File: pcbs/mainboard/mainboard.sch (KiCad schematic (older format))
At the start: 32 parts, among them J1 USB_B_Micro, SW1 SW_Push, SW2 SW_Push, U1 ATmega32U4-AU, U2 USBLC6-2SC6, U3 XC6206P332MR, U4 XC9572XL-10VQG44C, Y1 16MHz

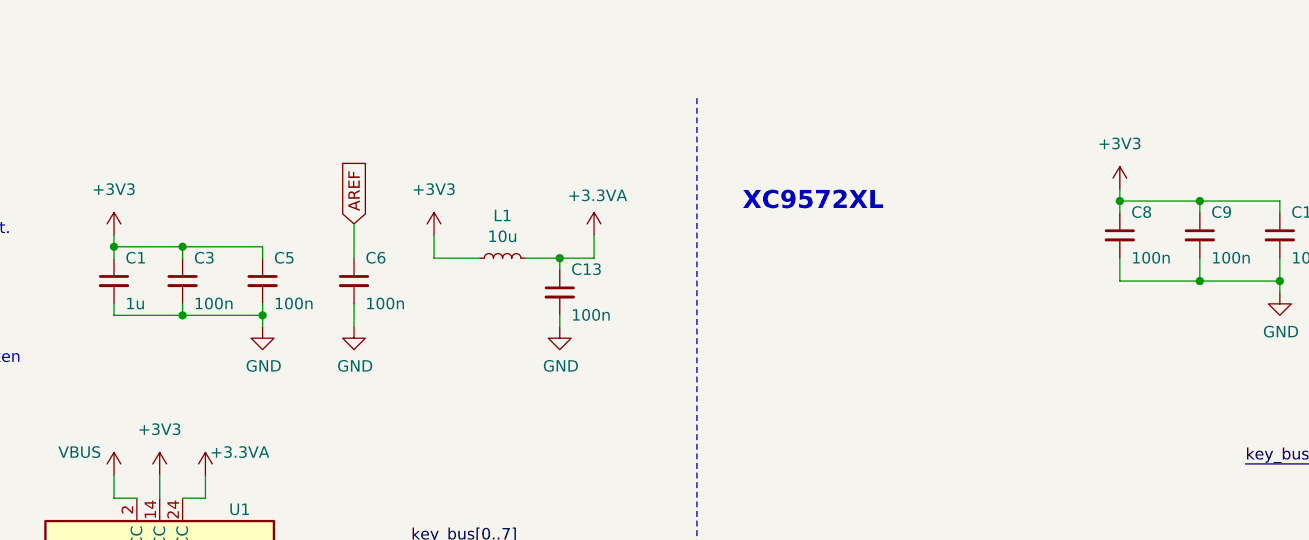
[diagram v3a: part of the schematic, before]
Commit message: Edit bypass capacitors, add JLC part for LDO
Both 32U4 and XC95 now bave 1uF bulk capacitor as well as a 100nF
for each VCC/GND pair.
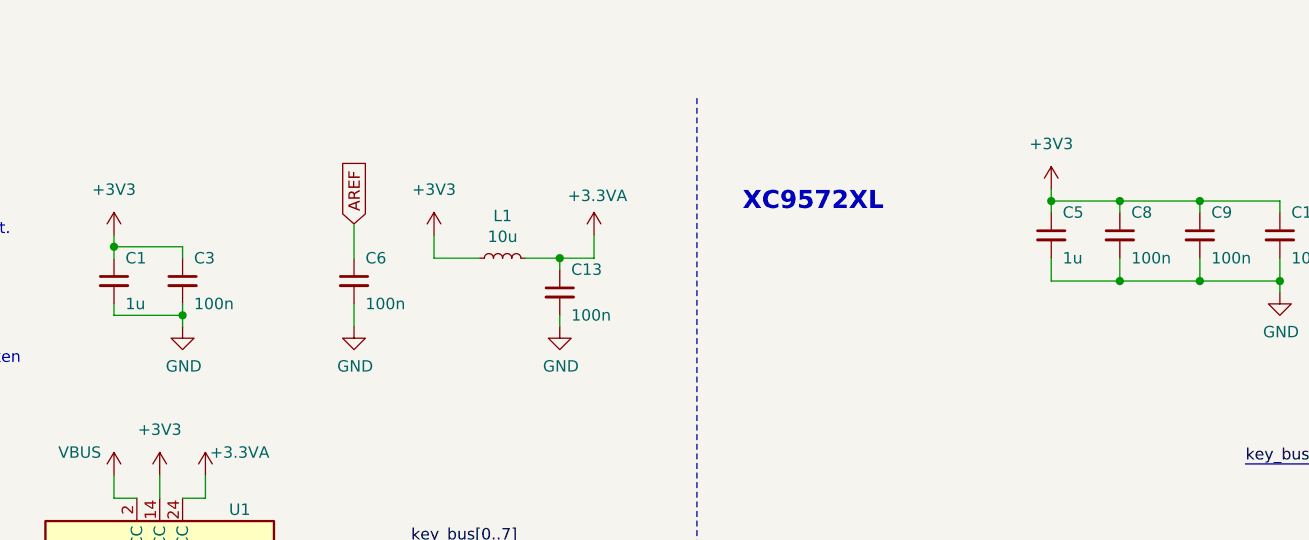
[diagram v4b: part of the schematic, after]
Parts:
- C1, C12, C7: JLCPCB Part # 0603 -> C15849
- C5: value 100n -> 1u; JLCPCB Part # C14663 -> C15849
- U3: JLCPCB Part # (none) -> C5446
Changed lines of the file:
@@
 F 2 "Capacitor_SMD:C_0603_1608Metric" H 2100 3900 50  0001 C CNN
 F 3 "~" H 2100 3900 50  0001 C CNN
-F 4 "0603" H 2100 3900 50  0001 C CNN "JLCPCB Part #"
+F 4 "C15849" H 2100 3900 50  0001 C CNN "JLCPCB Part #"
 	1    2100 3900
 	1    0    0    -1
@@
 F 2 "Capacitor_SMD:C_0603_1608Metric" H 2600 1200 50  0001 C CNN
 F 3 "~" H 2600 1200 50  0001 C CNN
-F 4 "0603" H 2600 1200 50  0001 C CNN "JLCPCB Part #"
+F 4 "C15849" H 2600 1200 50  0001 C CNN "JLCPCB Part #"
 	1    2600 1200
 	-1   0    0    -1
@@
 L power:GND #PWR06
 U 1 1 613BDE2B
-P 3250 1400
-F 0 "#PWR06" H 3250 1150 50  0001 C CNN
-F 1 "GND" H 3255 1227 50  0000 C CNN
-F 2 "" H 3250 1400 50  0001 C CNN
-F 3 "" H 3250 1400 50  0001 C CNN
-	1    3250 1400
+P 2900 1400
+F 0 "#PWR06" H 2900 1150 50  0001 C CNN
+F 1 "GND" H 2905 1227 50  0000 C CNN
+F 2 "" H 2900 1400 50  0001 C CNN
+F 3 "" H 2900 1400 50  0001 C CNN
+	1    2900 1400
 	1    0    0    -1
 $EndComp
@@
 	2600 1300 2600 1350
 Wire Wire Line
-	3250 1400 3250 1350
+	2900 1400 2900 1350
 Wire Wire Line
 	2900 1050 2900 1100
@@
 L power:+3V3 #PWR021
 U 1 1 6140CB03
-P 7000 800
-F 0 "#PWR021" H 7000 650 50  0001 C CNN
-F 1 "+3V3" H 7000 1000 50  0000 C CNN
-F 2 "" H 7000 800 50  0001 C CNN
-F 3 "" H 7000 800 50  0001 C CNN
-	1    7000 800
+P 6700 800
+F 0 "#PWR021" H 6700 650 50  0001 C CNN
+F 1 "+3V3" H 6700 1000 50  0000 C CNN
+F 2 "" H 6700 800 50  0001 C CNN
+F 3 "" H 6700 800 50  0001 C CNN
+	1    6700 800
 	-1   0    0    -1
 $EndComp
@@
 	1    0    0    -1
 $EndComp
-Wire Wire Line
-	7000 800  7000 850
 Wire Wire Line
 	7000 850  7350 850
@@
 F 2 "Package_TO_SOT_SMD:SOT-23" H 9150 5625 50  0001 C CIN
 F 3 "https://www.torexsemi.com/file/xc6206/XC6206.pdf" H 9150 5400 50  0001 C CNN
+F 4 "C5446" H 9150 5400 50  0001 C CNN "JLCPCB Part #"
 	1    9150 5400
 	1    0    0    -1
@@
 F 2 "Capacitor_SMD:C_0603_1608Metric" H 9650 5550 50  0001 C CNN
 F 3 "~" H 9650 5550 50  0001 C CNN
-F 4 "0603" H 9650 5550 50  0001 C CNN "JLCPCB Part #"
+F 4 "C15849" H 9650 5550 50  0001 C CNN "JLCPCB Part #"
 	1    9650 5550
 	1    0    0    -1
@@
 Wire Wire Line
 	10300 5150 10300 5300
-$Comp
-L Device:C_Small C5
-U 1 1 61680C17
-P 3250 1200
-F 0 "C5" H 3200 1300 50  0000 R CNN
-F 1 "100n" H 3200 1100 50  0000 R CNN
-F 2 "Capacitor_SMD:C_0603_1608Metric" H 3250 1200 50  0001 C CNN
-F 3 "~" H 3250 1200 50  0001 C CNN
-F 4 "C14663" H 3250 1200 50  0001 C CNN "JLCPCB Part #"
-	1    3250 1200
-	-1   0    0    -1
-$EndComp
-Wire Wire Line
-	2900 1050 3250 1050
-Wire Wire Line
-	3250 1050 3250 1100
-Connection ~ 2900 1050
 Wire Wire Line
 	2600 1350 2900 1350
-Wire Wire Line
-	3250 1300 3250 1350
-Connection ~ 3250 1350
 Wire Wire Line
 	2900 1300 2900 1350
 Connection ~ 2900 1350
-Wire Wire Line
-	2900 1350 3250 1350
 $Sheet
 S 12200 150  2550 1250
@@
 	1    0    0    -1
 $EndComp
-Wire Bus Line
-	3950 2400 3950 3550
-Wire Bus Line
-	8100 2000 8100 2700
-Wire Bus Line
-	3900 2350 3900 3250
 Wire Wire Line
 	2300 6600 2300 6700
@@
 	0    -1   -1   0
 $EndComp
+$Comp
+L Device:C_Small C5
+U 1 1 6168A0CD
+P 6700 1000
+F 0 "C5" H 6650 1100 50  0000 R CNN
+F 1 "1u" H 6650 900 50  0000 R CNN
+F 2 "Capacitor_SMD:C_0603_1608Metric" H 6700 1000 50  0001 C CNN
+F 3 "~" H 6700 1000 50  0001 C CNN
+F 4 "C15849" H 6700 1000 50  0001 C CNN "JLCPCB Part #"
+	1    6700 1000
+	-1   0    0    -1
+$EndComp
+Wire Wire Line
+	6700 850  6700 800
+Wire Wire Line
+	6700 850  7000 850
+Wire Wire Line
+	6700 900  6700 850
+Connection ~ 6700 850
+Wire Wire Line
+	6700 1100 6700 1200
+Wire Wire Line
+	6700 1200 7000 1200
+Wire Bus Line
+	3950 2400 3950 3550
+Wire Bus Line
+	8100 2000 8100 2700
+Wire Bus Line
+	3900 2350 3900 3250
+Connection ~ 7000 1200
 $EndSCHEMATC

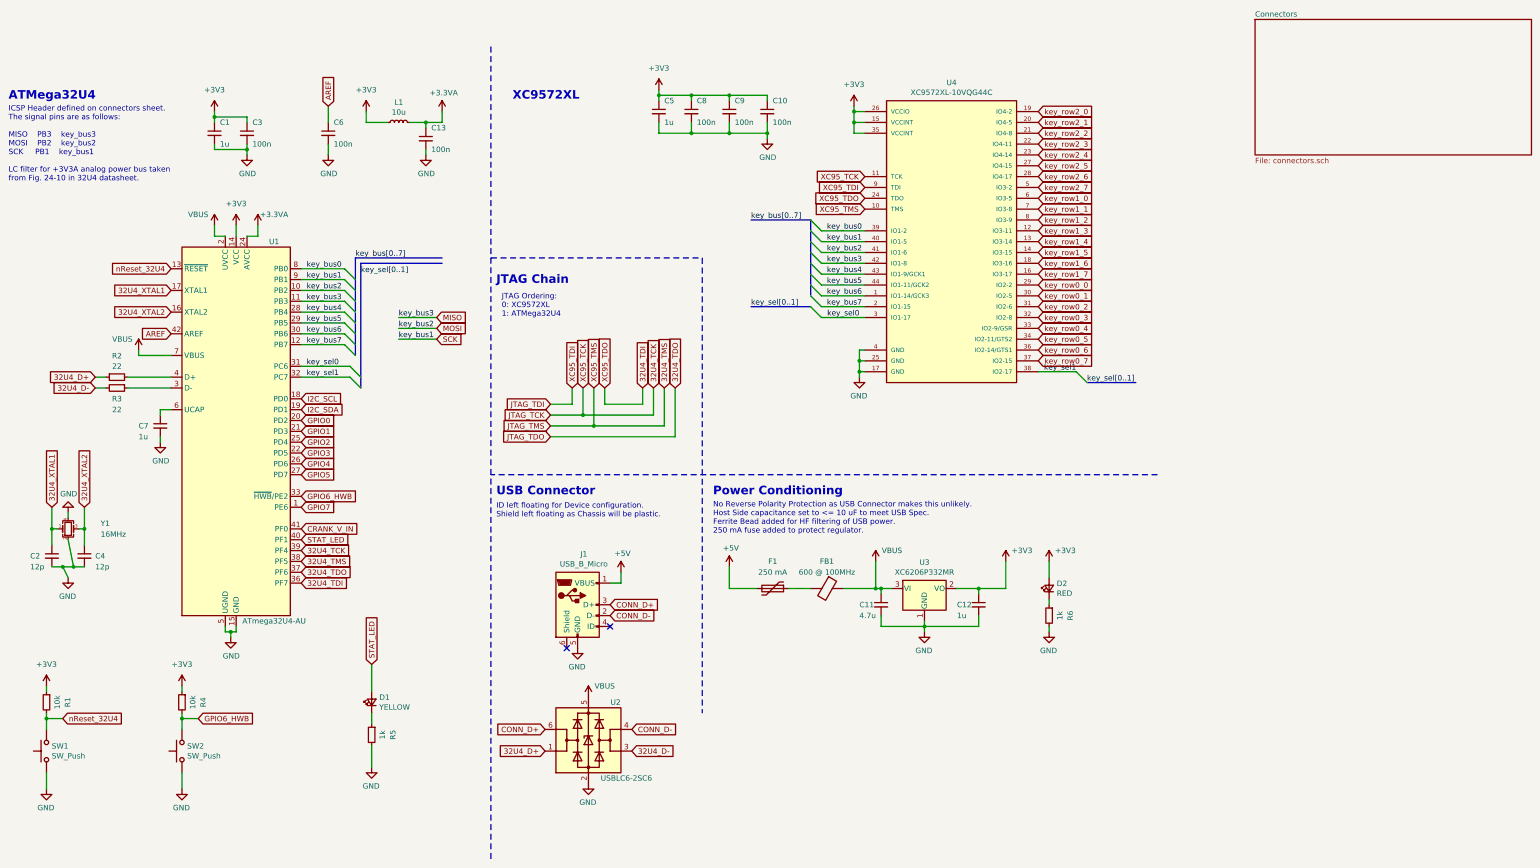
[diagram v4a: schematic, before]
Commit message: Add first draft of mainboard layout
Change pinout of XC95 to better link to the key_row screw terminals.

Change ordering of some signals on screw terminals and JTAG header
to allow more sensible routing.

Revise mounting hole scheme to only place one between the two rows
of terminal blocks rather than at each corner on the top.
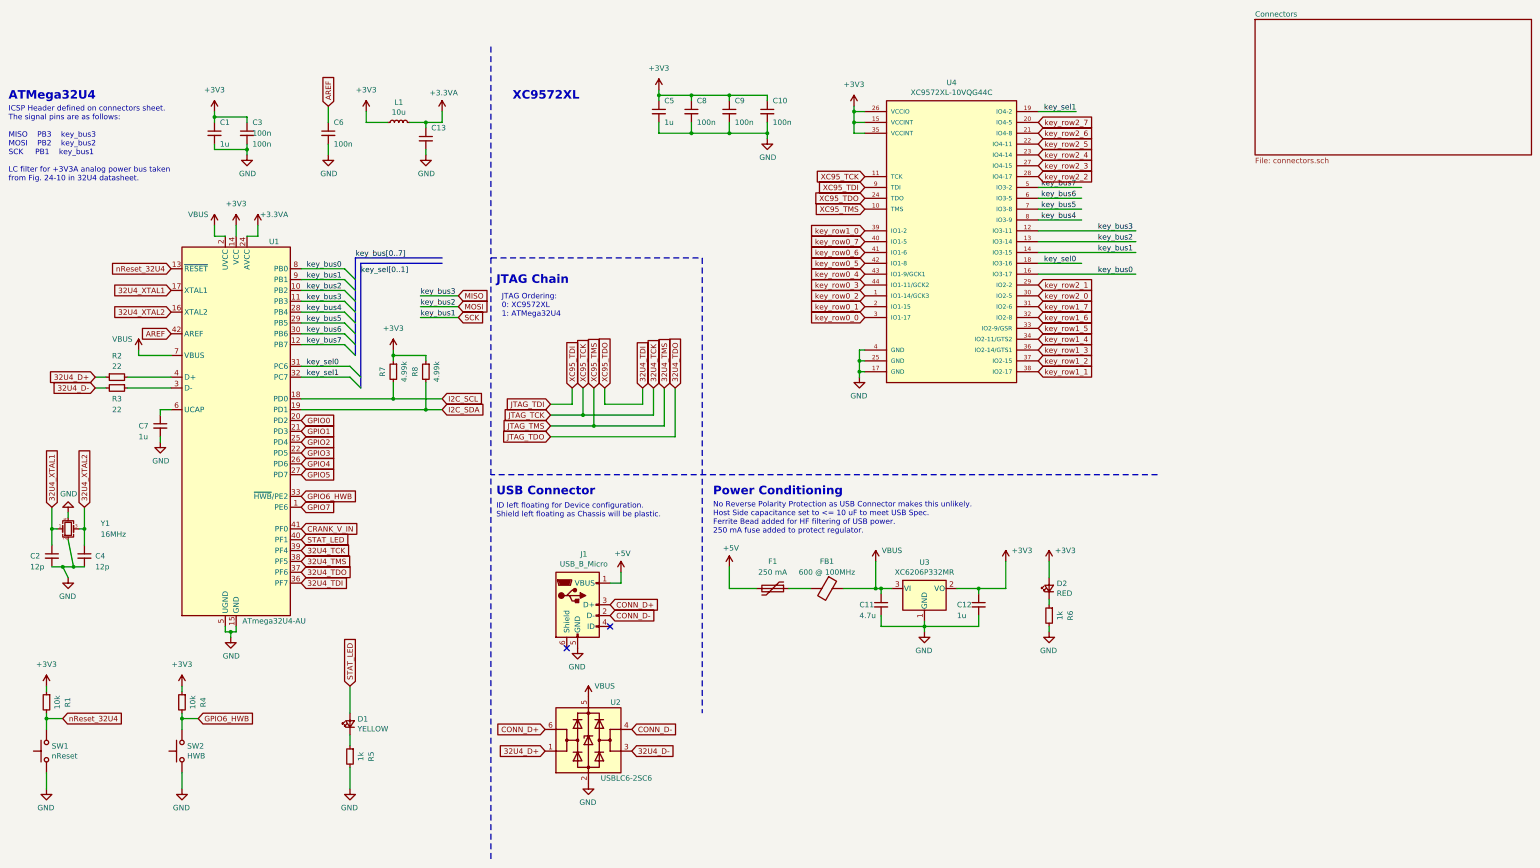
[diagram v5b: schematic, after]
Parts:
- added R7, R8: 4.99k, Resistor_SMD:R_0603_1608Metric, symbol Device:R_Small
- SW1: value SW_Push -> nReset
- SW2: value SW_Push -> HWB
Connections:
- wire segments 150 -> 160
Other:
- moved on the sheet: D1, R5

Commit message: Add first draft of mainboard routing
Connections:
- net labels added: D+, D-
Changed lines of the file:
@@
 XC95_TMS
 Wire Wire Line
-	10600 2400 10200 2400
+	10600 1000 10200 1000
 Wire Wire Line
 	10200 1700 10600 1700
@@
 Wire Wire Line
 	10200 2000 10600 2000
-Text Label 10550 2000 2    50   ~ 0
+Text Label 10600 2000 2    50   ~ 0
 key_bus4
-Text Label 10550 1900 2    50   ~ 0
+Text Label 10600 1900 2    50   ~ 0
 key_bus5
-Text Label 10550 1800 2    50   ~ 0
+Text Label 10600 1800 2    50   ~ 0
 key_bus6
-Text Label 10550 1700 2    50   ~ 0
+Text Label 10600 1700 2    50   ~ 0
 key_bus7
 Text GLabel 8600 2900 0    50   Input ~ 0
@@
 Text GLabel 8600 2400 0    50   Input ~ 0
 key_row0_5
+Text GLabel 8600 2200 0    50   Input ~ 0
+key_row0_6
 Text GLabel 8600 2300 0    50   Input ~ 0
-key_row0_6
-Text GLabel 8600 2200 0    50   Input ~ 0
 key_row0_7
 Text GLabel 8600 2100 0    50   Input ~ 0
@@
 Text GLabel 10200 1100 2    50   Input ~ 0
 key_row2_7
-Text Label 10550 2400 2    50   ~ 0
+Text Label 10600 1000 2    50   ~ 0
 key_sel0
-Text Label 10550 1000 2    50   ~ 0
-key_sel1
-Wire Wire Line
-	10200 1000 10550 1000
 Wire Notes Line
 	11300 4350 5150 4350
@@
 Wire Wire Line
 	4550 3750 3400 3750
-Wire Wire Line
-	10200 2300 11100 2300
-Wire Wire Line
-	10200 2200 11100 2200
 Text GLabel 10200 2900 2    50   Input ~ 0
 key_row1_6
@@
 Text GLabel 10200 3200 2    50   Input ~ 0
 key_row1_3
-Wire Wire Line
-	10200 2500 11100 2500
-Wire Wire Line
-	10200 2100 11100 2100
-Text Label 10750 2500 0    50   ~ 0
-key_bus0
-Text Label 10750 2300 0    50   ~ 0
+Text Label 10600 2200 2    50   ~ 0
 key_bus1
-Text Label 10750 2200 0    50   ~ 0
+Text Label 10600 2300 2    50   ~ 0
 key_bus2
-Text Label 10750 2100 0    50   ~ 0
+Text Label 10600 2500 2    50   ~ 0
 key_bus3
-Wire Bus Line
-	3950 2400 3950 3550
-Wire Bus Line
-	3900 2350 3900 3250
 $Comp
 L Device:C_Small C9
@@
 	1    0    0    -1
 $EndComp
+Text Label 10600 2100 2    50   ~ 0
+key_bus0
+Wire Wire Line
+	10200 2200 10600 2200
+Wire Wire Line
+	10200 2100 10600 2100
+Wire Wire Line
+	10200 2300 10600 2300
+Wire Wire Line
+	10200 2500 10600 2500
+Text Label 2000 3450 2    50   ~ 0
+D+
+Text Label 2000 3550 2    50   ~ 0
+D-
+Wire Wire Line
+	10200 2400 10550 2400
+Text Label 10550 2400 2    50   ~ 0
+key_sel1
+Wire Bus Line
+	3950 2400 3950 3550
+Wire Bus Line
+	3900 2350 3900 3250
 $EndSCHEMATC

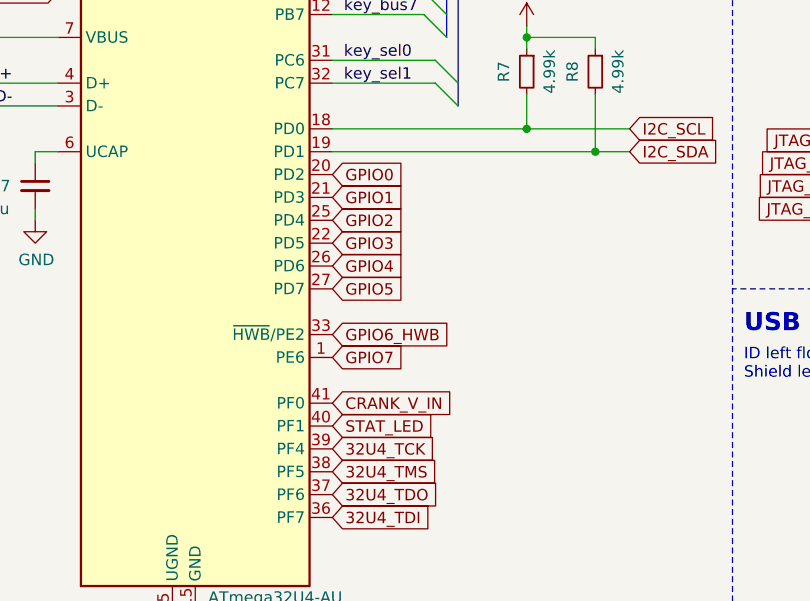
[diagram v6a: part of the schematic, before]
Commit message: Add useful/readabhle silkscreen
Swap pins on CRANK_V_IN terminal block to shorten track
and match the polarity of other +/- terminal blocks.
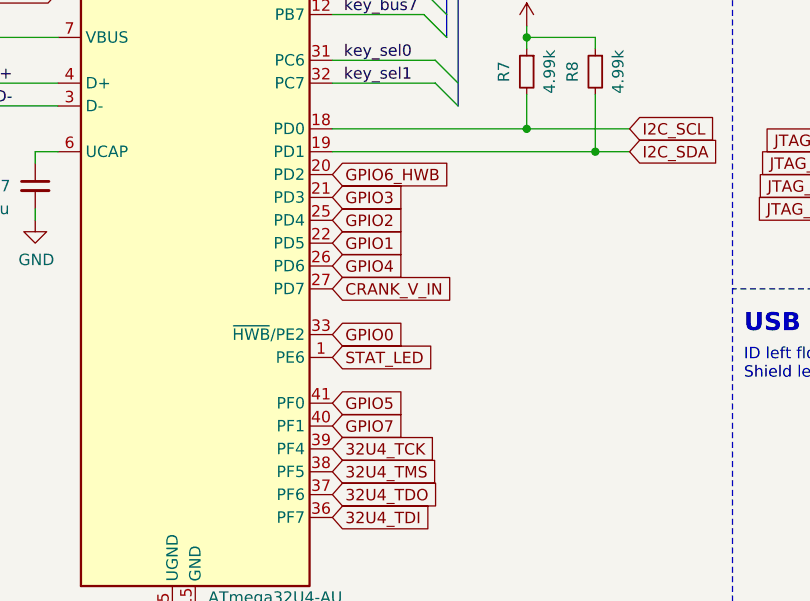
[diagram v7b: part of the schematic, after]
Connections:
- net CRANK_V_IN: now also U1.27 (PD7); no longer U1.41 (PF0)
- net GPIO0: now also U1.33 (~HWB~/PE2); no longer U1.20 (PD2)
- net GPIO1: now also U1.22 (PD5); no longer U1.21 (PD3)
- net GPIO3: now also U1.21 (PD3); no longer U1.22 (PD5)
- net GPIO5: now also U1.41 (PF0); no longer U1.27 (PD7)
- net GPIO6_HWB: now also U1.20 (PD2); no longer U1.33 (~HWB~/PE2)
- net GPIO7: now also U1.40 (PF1); no longer U1.1 (PE6)
- net STAT_LED: now also U1.1 (PE6); no longer U1.40 (PF1)
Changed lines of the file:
@@
 Text GLabel 4700 3750 2    50   Input ~ 0
 I2C_SDA
-Text GLabel 3400 4850 2    50   Input ~ 0
+Text GLabel 3400 4350 2    50   Input ~ 0
 CRANK_V_IN
 Text GLabel 3400 5350 2    50   Input ~ 0
@@
 Text GLabel 3400 5050 2    50   Input ~ 0
 32U4_TCK
-Text GLabel 3400 4950 2    50   Input ~ 0
+Text GLabel 3400 4650 2    50   Input ~ 0
 STAT_LED
-Text GLabel 3400 3850 2    50   Input ~ 0
+Text GLabel 3400 4550 2    50   Input ~ 0
 GPIO0
-Text GLabel 3400 3950 2    50   Input ~ 0
+Text GLabel 3400 4150 2    50   Input ~ 0
 GPIO1
 Text GLabel 3400 4050 2    50   Input ~ 0
 GPIO2
-Text GLabel 3400 4150 2    50   Input ~ 0
+Text GLabel 3400 3950 2    50   Input ~ 0
 GPIO3
 Text GLabel 3400 4250 2    50   Input ~ 0
 GPIO4
-Text GLabel 3400 4350 2    50   Input ~ 0
+Text GLabel 3400 4850 2    50   Input ~ 0
 GPIO5
-Text GLabel 3400 4550 2    50   Input ~ 0
+Text GLabel 3400 3850 2    50   Input ~ 0
 GPIO6_HWB
-Text GLabel 3400 4650 2    50   Input ~ 0
+Text GLabel 3400 4950 2    50   Input ~ 0
 GPIO7
 $Comp
